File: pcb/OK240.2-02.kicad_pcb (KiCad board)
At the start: 2 copper layers, 325.1 x 180.3 mm, 325 parts, among them X2 KEYBOARD, X3 LPT, X5 X5, X6 POWER

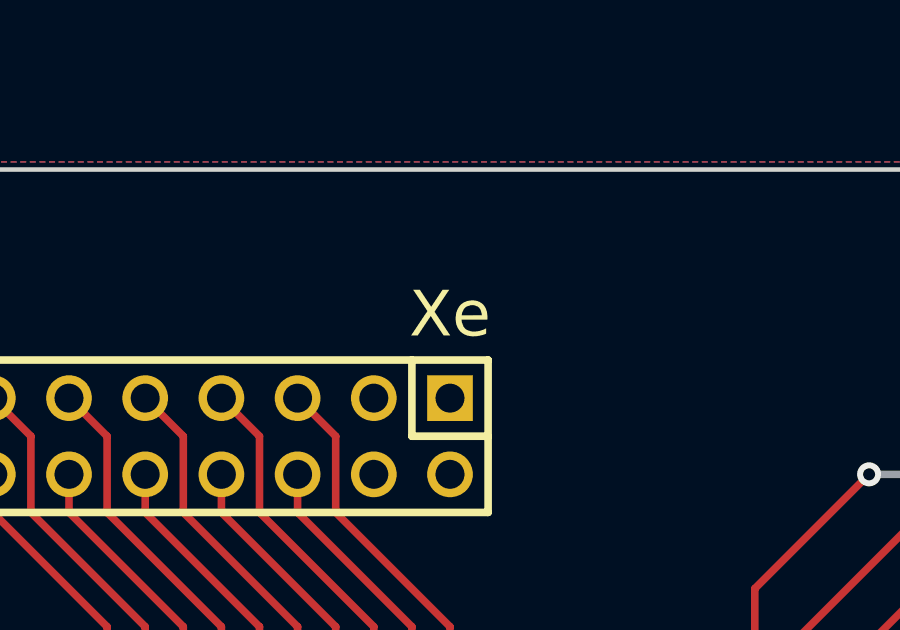
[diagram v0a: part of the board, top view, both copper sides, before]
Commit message: Add right angle IDC 30-pin connector 3D models
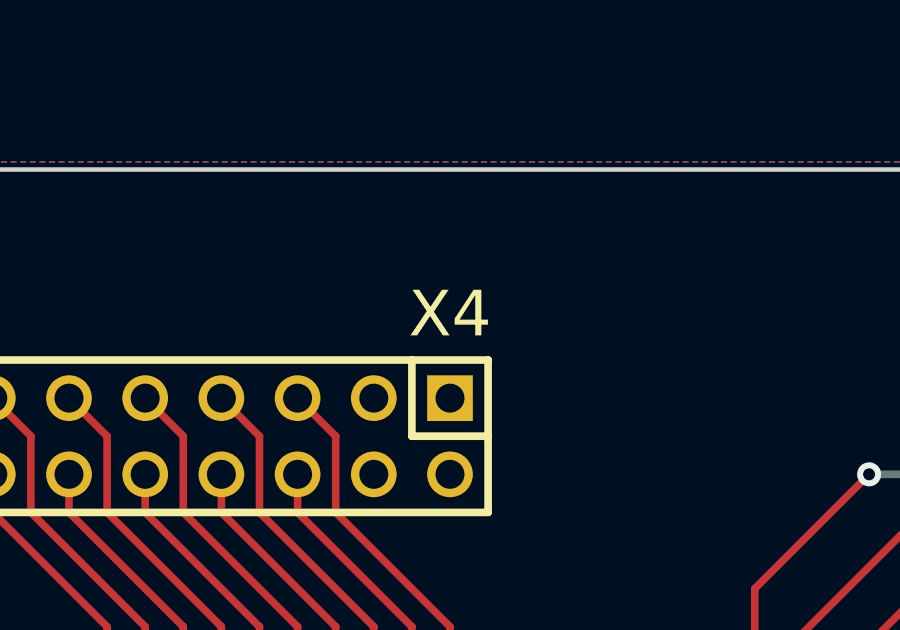
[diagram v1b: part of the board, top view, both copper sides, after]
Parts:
- X4: renamed from Xe; value X4 -> FLOPPY
- X5: value X5 -> (none)
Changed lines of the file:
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@@
 			)
 		)
-		(property "Value" "X5"
+		(property "Value" ""
 			(at 3.302 1.524 0)
 			(layer "F.Fab")
@@
 		)
 		(embedded_fonts no)
-		(model ":KICAD7_3DMODEL_DIR:Connector_PinHeader_2.54mm.3dshapes/PinHeader_2x15_P2.54mm_Vertical.step"
-			(hide yes)
-			(offset
-				(xyz 0 0 0)
-			)
-			(scale
-				(xyz 1 1 1)
-			)
-			(rotate
-				(xyz 0 0 90)
-			)
-		)
-		(model ":KICAD7_3DMODEL_DIR:Connector_IDC.3dshapes/IDC-Header_2x15_P2.54mm_Horizontal.step"
+		(model "${KICAD9_3DMODEL_DIR}/Connector_IDC.3dshapes/IDC-Header_2x15_P2.54mm_Horizontal.step"
 			(offset
 				(xyz -35.56 -2.54 0)
@@
 			)
 			(rotate
-				(xyz 0 0 -90)
+				(xyz -0 -0 -90)
 			)
 		)
@@
 		)
 		(embedded_fonts no)
-		(model ":KICAD7_3DMODEL_DIR:Connector_PinHeader_2.54mm.3dshapes/PinHeader_2x15_P2.54mm_Vertical.step"
-			(hide yes)
-			(offset
-				(xyz 0 0 0)
-			)
-			(scale
-				(xyz 1 1 1)
-			)
-			(rotate
-				(xyz 0 0 90)
-			)
-		)
-		(model ":KICAD7_3DMODEL_DIR:Connector_IDC.3dshapes/IDC-Header_2x15_P2.54mm_Horizontal.step"
+		(model "${KICAD9_3DMODEL_DIR}/Connector_IDC.3dshapes/IDC-Header_2x15_P2.54mm_Horizontal.step"
 			(offset
 				(xyz -35.56 -2.54 0)
@@
 			)
 			(rotate
-				(xyz 0 0 -90)
+				(xyz -0 -0 -90)
 			)
 		)
@@
 		(at 105.9688 65.786)
 		(descr "HEADER30_2.fp_dup2")
-		(property "Reference" "Xe"
+		(property "Reference" "X4"
 			(at 0 -2.794 0)
 			(layer "F.SilkS")
@@
 			)
 		)
-		(property "Value" "X4"
+		(property "Value" "FLOPPY"
 			(at 3.302 1.524 0)
 			(layer "F.Fab")
@@
 		)
 		(embedded_fonts no)
-		(model ":KICAD7_3DMODEL_DIR:Connector_PinHeader_2.54mm.3dshapes/PinHeader_2x15_P2.54mm_Vertical.step"
-			(hide yes)
-			(offset
-				(xyz 0 0 0)
-			)
-			(scale
-				(xyz 1 1 1)
-			)
-			(rotate
-				(xyz 0 0 90)
-			)
-		)
-		(model ":KICAD7_3DMODEL_DIR:Connector_IDC.3dshapes/IDC-Header_2x15_P2.54mm_Horizontal.step"
+		(model "${KICAD9_3DMODEL_DIR}/Connector_IDC.3dshapes/IDC-Header_2x15_P2.54mm_Horizontal.step"
 			(offset
 				(xyz -35.56 -2.54 0)
@@
 			)
 			(rotate
-				(xyz 0 0 -90)
+				(xyz -0 -0 -90)
 			)
 		)
